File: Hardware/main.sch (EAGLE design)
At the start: 26 parts, among them IC3 MEGA128-A, K1 DS2-L2-12V, T1 IRML5202, T2 IRML5202, T3 IRML5202

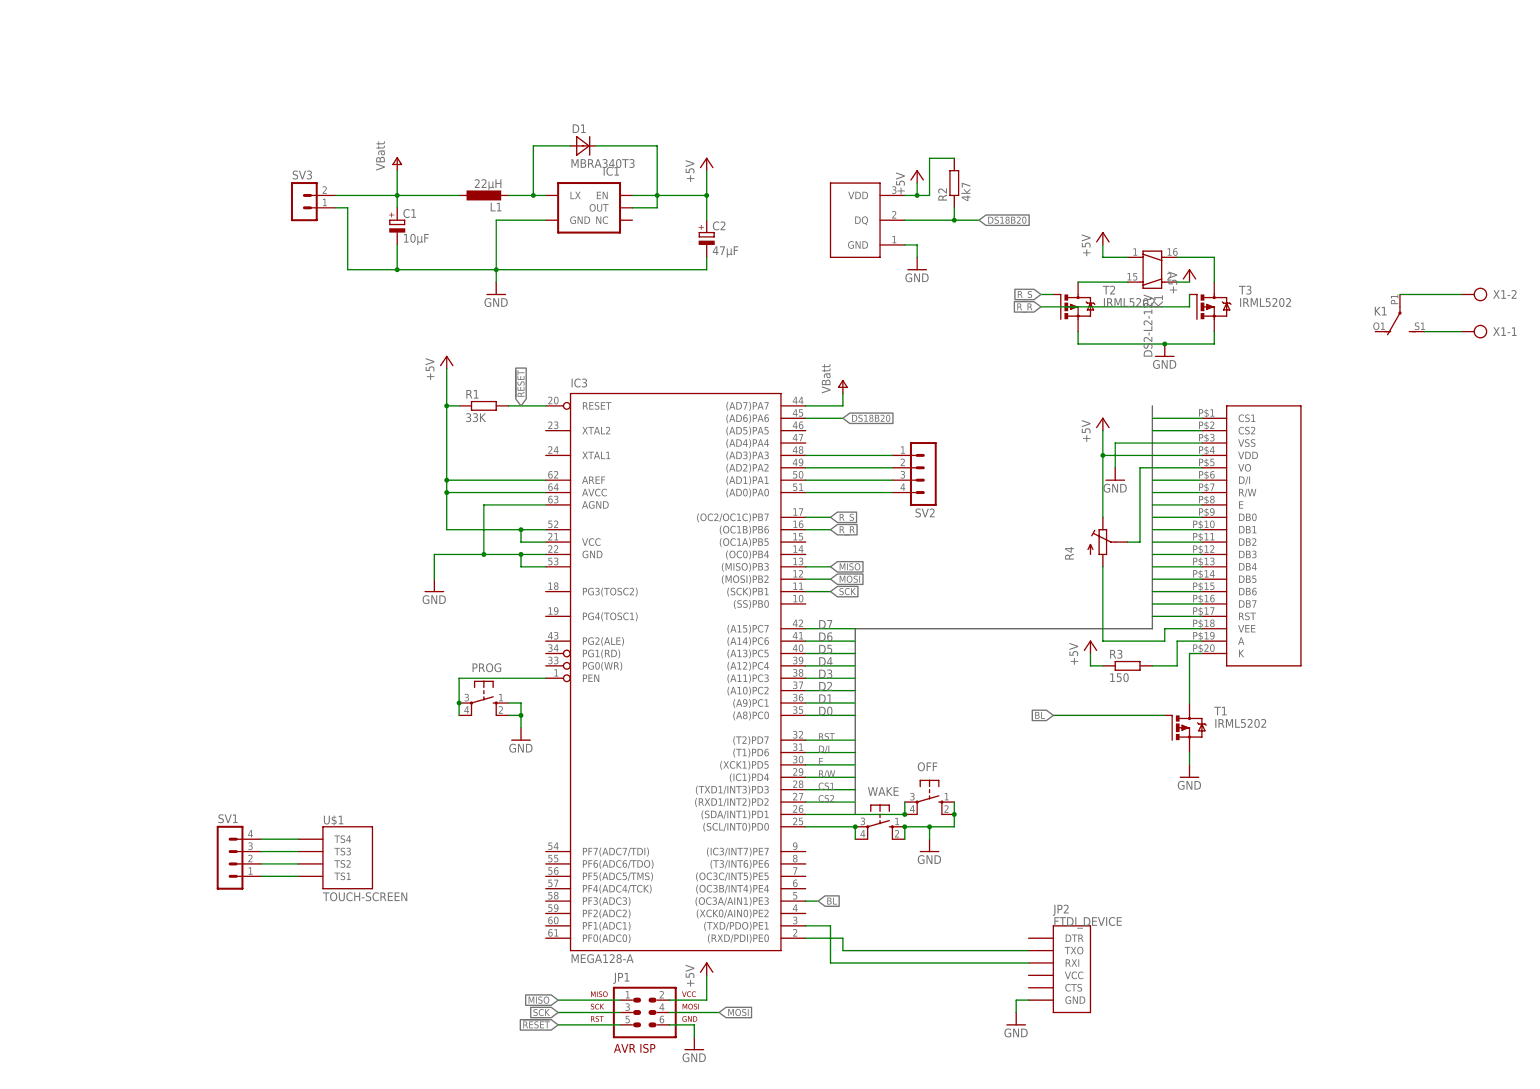
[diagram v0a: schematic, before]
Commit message: Added a ds1307
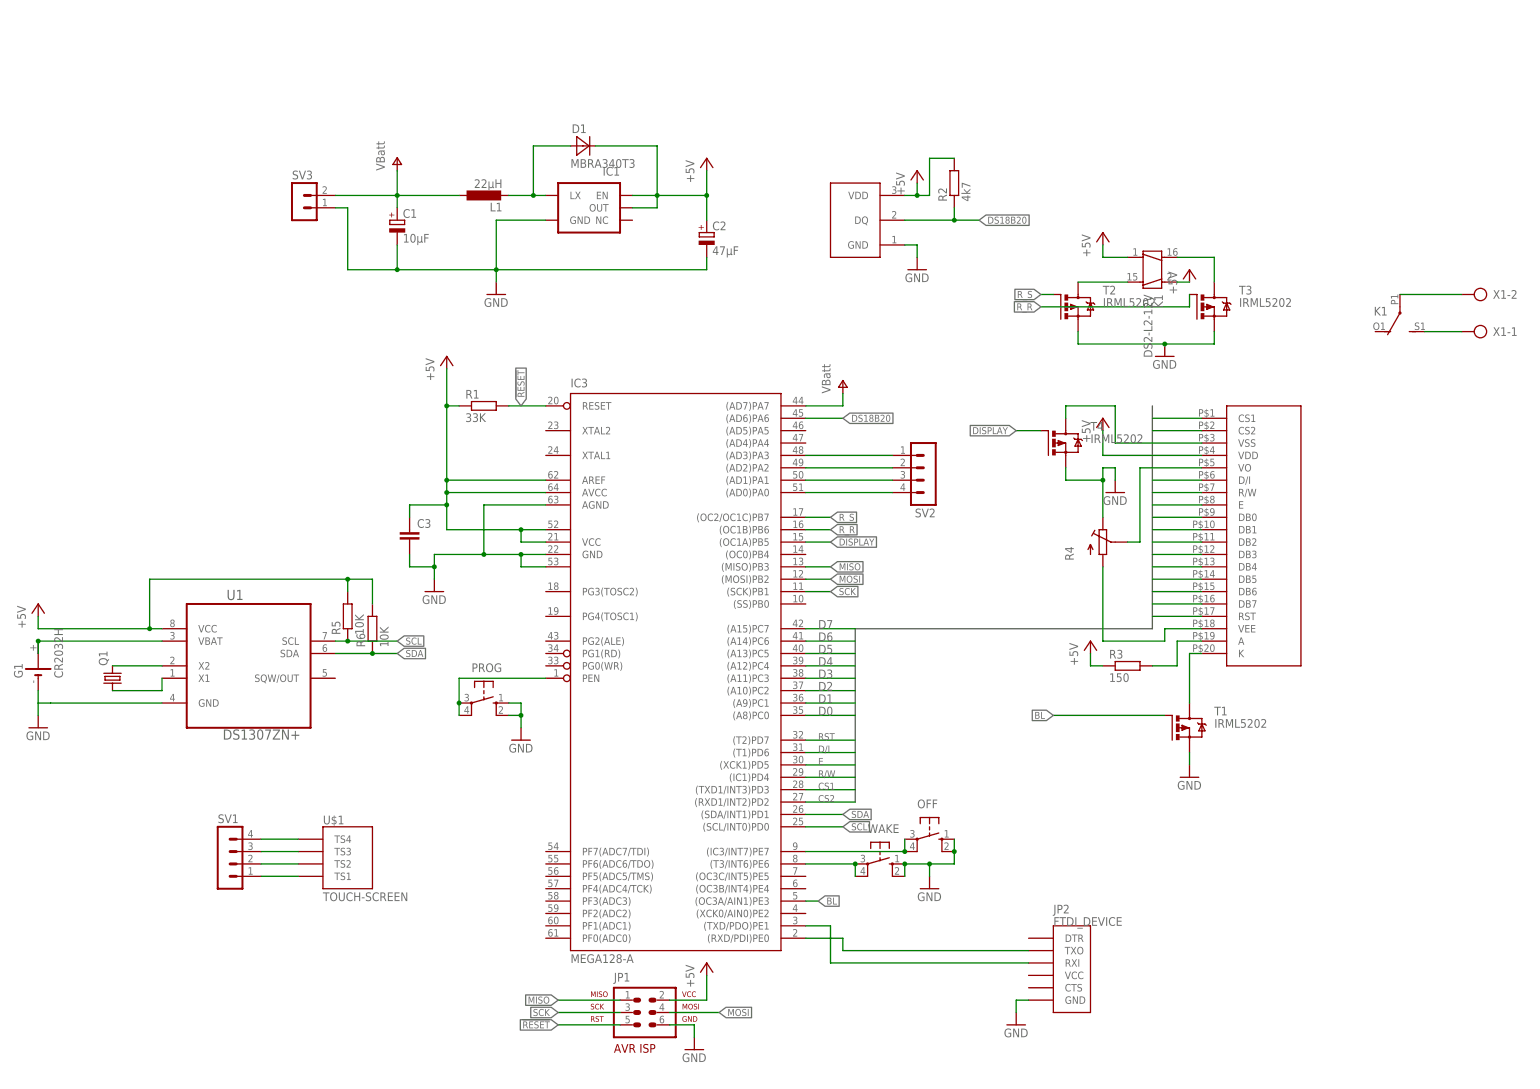
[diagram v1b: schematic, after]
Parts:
- added C3: (no value), rcl:C-EUC0805
- added G1: CR2032H, battery:CR2032H
- added Q1: (no value), crystal:CRYSTALTC26H
- added R5, R6: 10K, rcl:R-EU_R0805
- added T4: IRML5202, custom:IRML5202
- added U1: DS1307ZN+, custom:DS1307ZN+
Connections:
- new net DISPLAY: IC3.(OC1A)PB5, T4.G
- new net N$23: T4.S, U$2.VSS
- new net N$24: G1.+, G1.+@1, U1.VBAT
- new net N$26: Q1.1, U1.X1
- new net N$27: Q1.2, U1.X2
- new net SCL: IC3.(SCL/INT0)PD0, R5.1, U1.SCL
- new net SDA: IC3.(SDA/INT1)PD1, R6.1, U1.SDA
- net +5V: now also C3.1, R5.2, R6.2, U1.VCC; no longer R4.1
- net GND: now also C3.2, G1.-, R4.1, T4.D, U1.GND; no longer U$2.VSS
- net N$10: now also IC3.(T3/INT6)PE6; no longer IC3.(SCL/INT0)PD0
- net N$16: now also IC3.(IC3/INT7)PE7; no longer IC3.(SDA/INT1)PD1
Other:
- moved on the sheet: OFF, WAKE

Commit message: Rotated the PCB, Added a button + LED
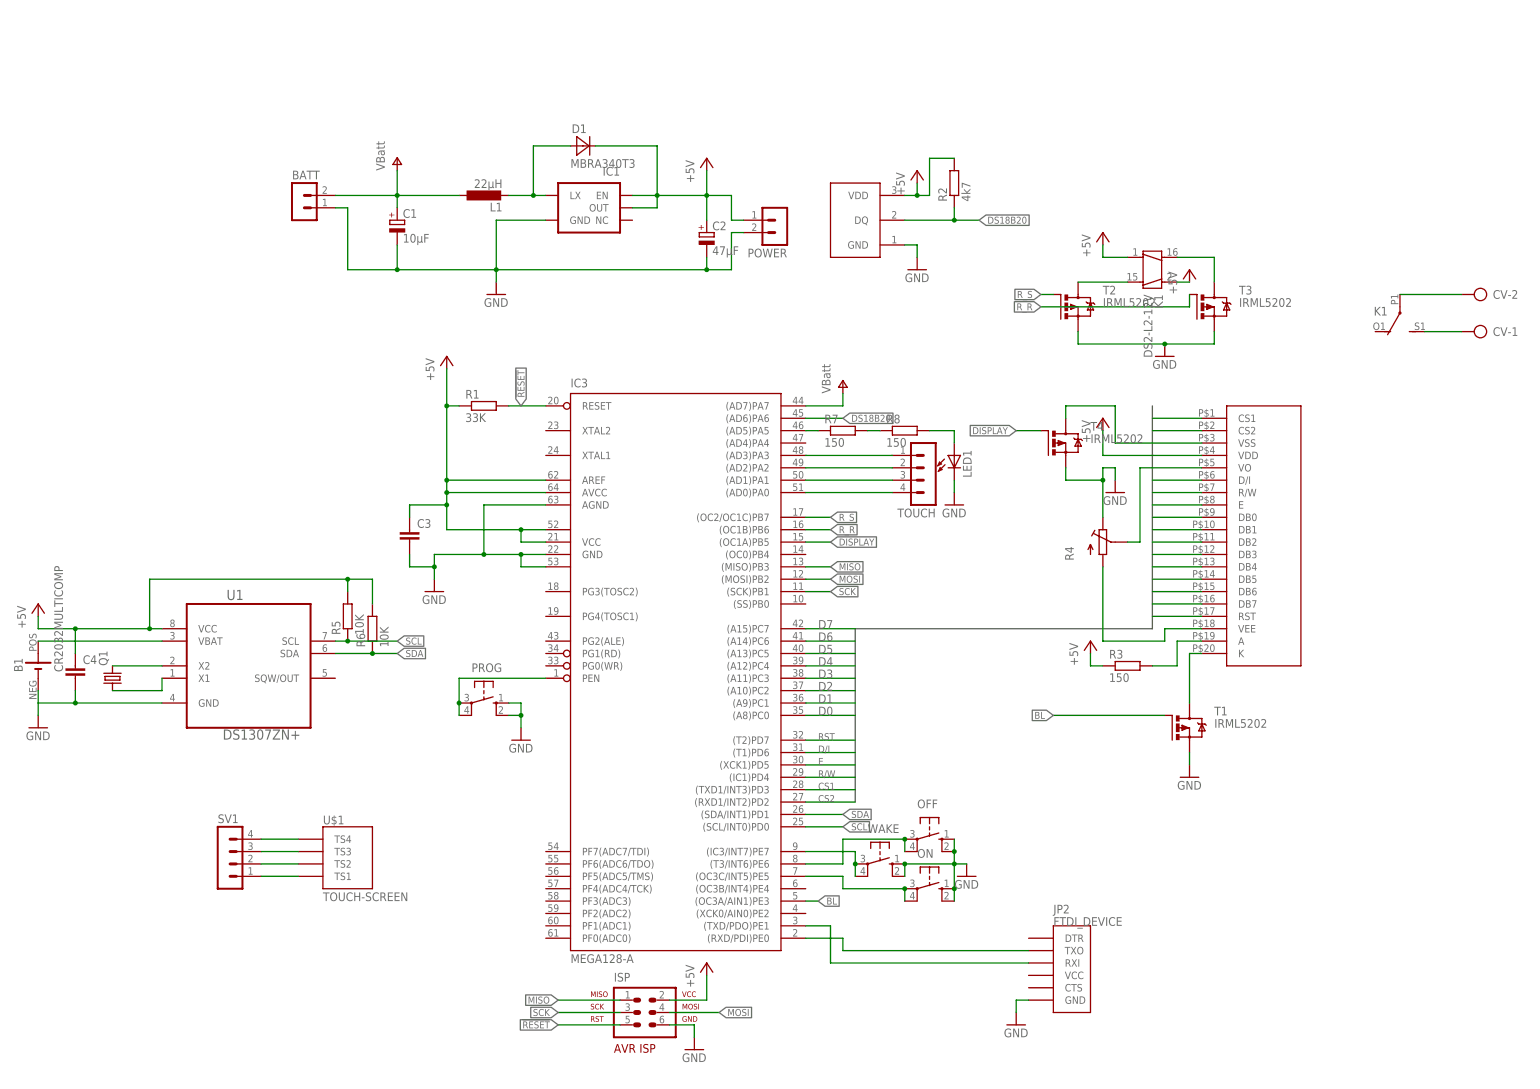
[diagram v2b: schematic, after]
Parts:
- removed G1: CR2032H, battery:CR2032H
- added B1: CR2032MULTICOMP, custom:CR2032MULTICOMP
- added C4: (no value), rcl:C-EUC0805
- added LED1: (no value), led:LEDSML1206
- added ON: (no value), switch-omron:10-XX
- added POWER: MA02-1, con-lstb:MA02-1
- added R7, R8: 150, rcl:R-EU_R0805
- Q1: device crystal:CRYSTALTC26H -> crystal:CRYSTALTC26V
- renumbered JP1 to ISP, SV2 to TOUCH, SV3 to BATT, U$3 to DS1820, X1 to CV
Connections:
- new net N$28: IC3.(OC3C/INT5)PE5, ON.P, ON.P1
- new net N$29: LED1.A, R8.2
- new net N$30: IC3.(AD5)PA5, R7.1
- new net N$31: R7.2, R8.1
- net +5V: now also C4.1, POWER.3
- net GND: now also B1.-, C4.2, LED1.C, ON.S, ON.S1, POWER.4; no longer G1.-
- net N$10: now also IC3.(IC3/INT7)PE7; no longer IC3.(T3/INT6)PE6
- net N$16: now also IC3.(T3/INT6)PE6; no longer IC3.(IC3/INT7)PE7
- net N$24: now also B1.+; no longer G1.+, G1.+@1

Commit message: Partially working firmware. It's just a test
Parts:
- added R9: 10K, rcl:R-EU_R0805
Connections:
- new net CV_ON: IC3.(OC0)PB4, K13.S, R9.2
- net +5V: now also K13.P
- net GND: now also R9.1
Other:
- moved on the sheet: CV-1, CV-2, K1
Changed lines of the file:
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@@
 <part name="C4" library="rcl" deviceset="C-EU" device="C0805"/>
 <part name="POWER" library="con-lstb" deviceset="MA02-1" device="" value=""/>
+<part name="P+12" library="supply1" deviceset="+5V" device=""/>
+<part name="R9" library="rcl" deviceset="R-EU_" device="R0805" value="10K"/>
+<part name="GND13" library="supply1" deviceset="GND" device=""/>
 </parts>
 <sheets>
@@
 <instance part="GND9" gate="1" x="142.24" y="104.14"/>
 <instance part="K1" gate="1" x="149.86" y="149.86" rot="R270"/>
-<instance part="K1" gate="2" x="200.66" y="142.24" rot="R180"/>
+<instance part="K1" gate="2" x="200.66" y="137.16" rot="R180"/>
 <instance part="T2" gate="G$1" x="132.08" y="142.24"/>
 <instance part="T3" gate="G$1" x="160.02" y="142.24"/>
@@
 <instance part="GND10" gate="1" x="152.4" y="132.08"/>
 <instance part="OFF" gate="1" x="104.14" y="33.02" rot="R270"/>
-<instance part="CV" gate="-1" x="218.44" y="137.16" rot="R180"/>
-<instance part="CV" gate="-2" x="218.44" y="144.78" rot="R180"/>
+<instance part="CV" gate="-1" x="218.44" y="132.08" rot="R180"/>
+<instance part="CV" gate="-2" x="218.44" y="139.7" rot="R180"/>
 <instance part="SV1" gate="1" x="-40.64" y="30.48"/>
 <instance part="TOUCH" gate="1" x="104.14" y="106.68" rot="R180"/>
@@
 <instance part="C4" gate="G$1" x="-71.12" y="68.58"/>
 <instance part="POWER" gate="G$1" x="73.66" y="157.48" rot="R180"/>
+<instance part="K1" gate="3" x="198.12" y="162.56" rot="R180"/>
+<instance part="P+12" gate="1" x="198.12" y="175.26"/>
+<instance part="R9" gate="G$1" x="208.28" y="152.4" rot="R90"/>
+<instance part="GND13" gate="1" x="208.28" y="142.24"/>
 </instances>
 <busses>
@@
 <pinref part="LED1" gate="G$1" pin="C"/>
 <wire x1="109.22" y1="104.14" x2="109.22" y2="106.68" width="0.1524" layer="91"/>
+</segment>
+<segment>
+<pinref part="GND13" gate="1" pin="GND"/>
+<pinref part="R9" gate="G$1" pin="1"/>
+<wire x1="208.28" y1="144.78" x2="208.28" y2="147.32" width="0.1524" layer="91"/>
 </segment>
 </net>
@@
 <junction x="-71.12" y="76.2"/>
 </segment>
+<segment>
+<pinref part="P+12" gate="1" pin="+5V"/>
+<pinref part="K1" gate="3" pin="P"/>
+<wire x1="198.12" y1="172.72" x2="198.12" y2="165.1" width="0.1524" layer="91"/>
+</segment>
 </net>
 <net name="D0" class="0">
@@
 <pinref part="CV" gate="-2" pin="KL"/>
 <pinref part="K1" gate="2" pin="P"/>
-<wire x1="213.36" y1="144.78" x2="200.66" y2="144.78" width="0.1524" layer="91"/>
+<wire x1="213.36" y1="139.7" x2="200.66" y2="139.7" width="0.1524" layer="91"/>
 </segment>
 </net>
@@
 <pinref part="CV" gate="-1" pin="KL"/>
 <pinref part="K1" gate="2" pin="S"/>
-<wire x1="213.36" y1="137.16" x2="205.74" y2="137.16" width="0.1524" layer="91"/>
+<wire x1="213.36" y1="132.08" x2="205.74" y2="132.08" width="0.1524" layer="91"/>
 </segment>
 </net>
@@
 </segment>
 </net>
+<net name="CV_ON" class="0">
+<segment>
+<pinref part="K1" gate="3" pin="S"/>
+<wire x1="203.2" y1="157.48" x2="208.28" y2="157.48" width="0.1524" layer="91"/>
+<pinref part="R9" gate="G$1" pin="2"/>
+<wire x1="208.28" y1="157.48" x2="213.36" y2="157.48" width="0.1524" layer="91"/>
+<junction x="208.28" y="157.48"/>
+<label x="213.36" y="157.48" size="1.778" layer="95" xref="yes"/>
+</segment>
+<segment>
+<pinref part="IC3" gate="G$1" pin="(OC0)PB4"/>
+<wire x1="78.74" y1="91.44" x2="83.82" y2="91.44" width="0.1524" layer="91"/>
+<label x="83.82" y="91.44" size="1.4224" layer="95" xref="yes"/>
+</segment>
+</net>
